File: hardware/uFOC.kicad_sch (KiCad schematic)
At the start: 0 parts

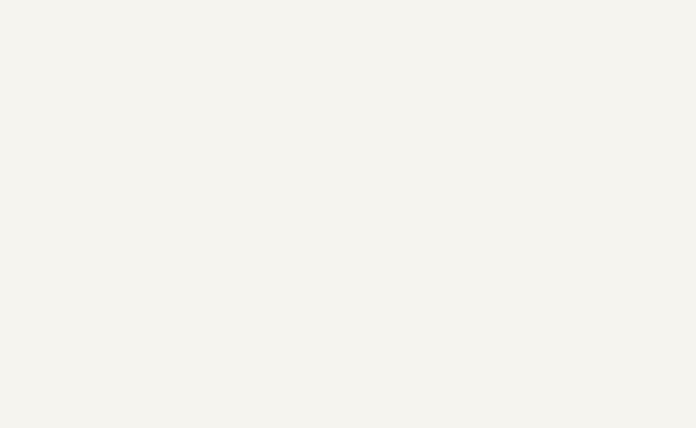
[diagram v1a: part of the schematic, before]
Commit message: Simplified sensing, added some power layout.
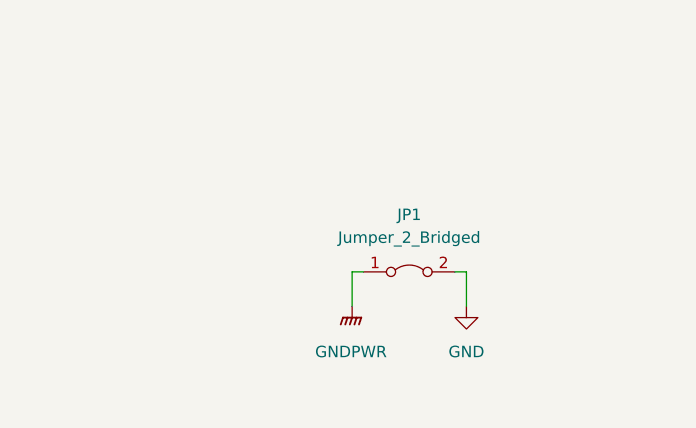
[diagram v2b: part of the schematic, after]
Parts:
- added JP1: Jumper_2_Bridged, symbol Jumper:Jumper_2_Bridged
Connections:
- new net GND: JP1.2 (B)
- new net GNDPWR: JP1.1 (A)
